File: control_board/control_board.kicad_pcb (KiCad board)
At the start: 2 copper layers, 50.8 x 76.2 mm, 38 parts, among them J1 Conn_01x08_Male, K1 G5Q-1A, Q1 Q_NPN_BEC, U1 MC78M05_TO252, U2 TSR_1-24120, U3 74LS02, U4 74LS02, U5 Conn_01x08_Male

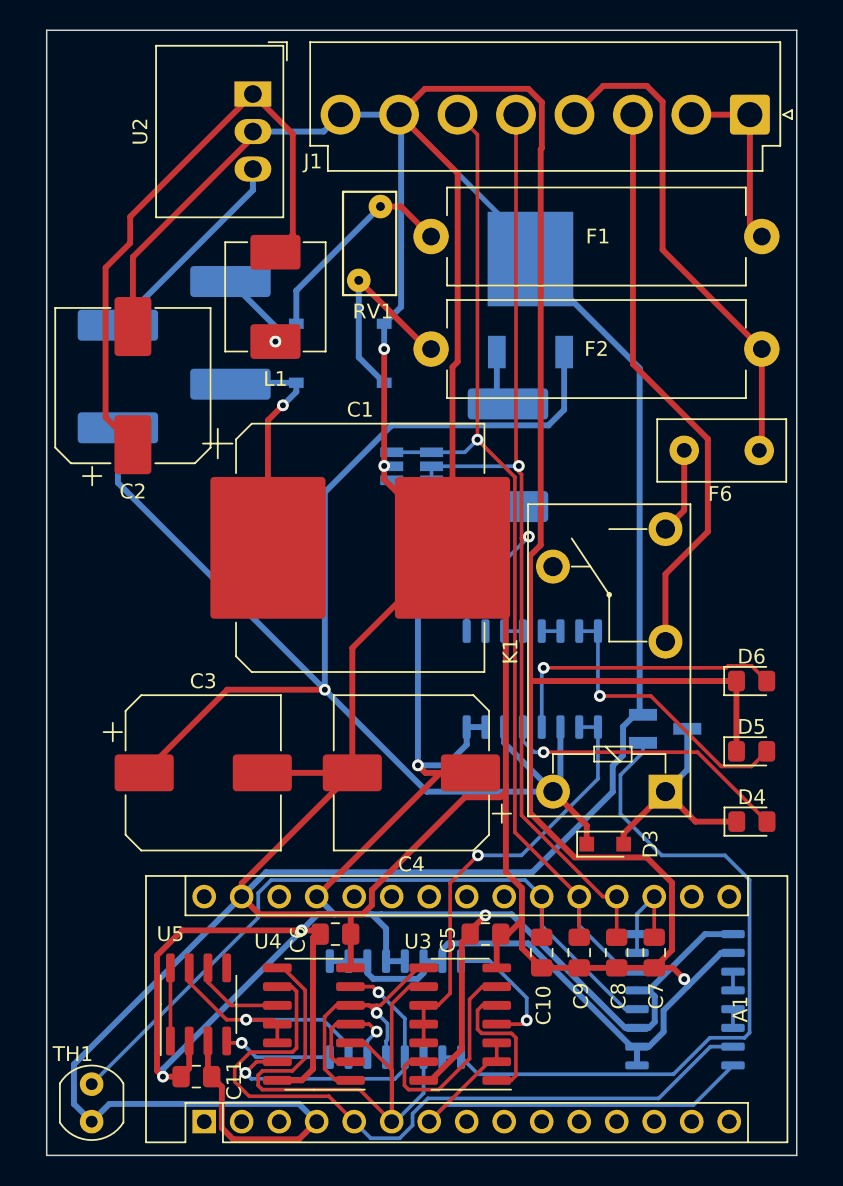
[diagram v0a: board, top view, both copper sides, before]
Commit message: Optimize some traces
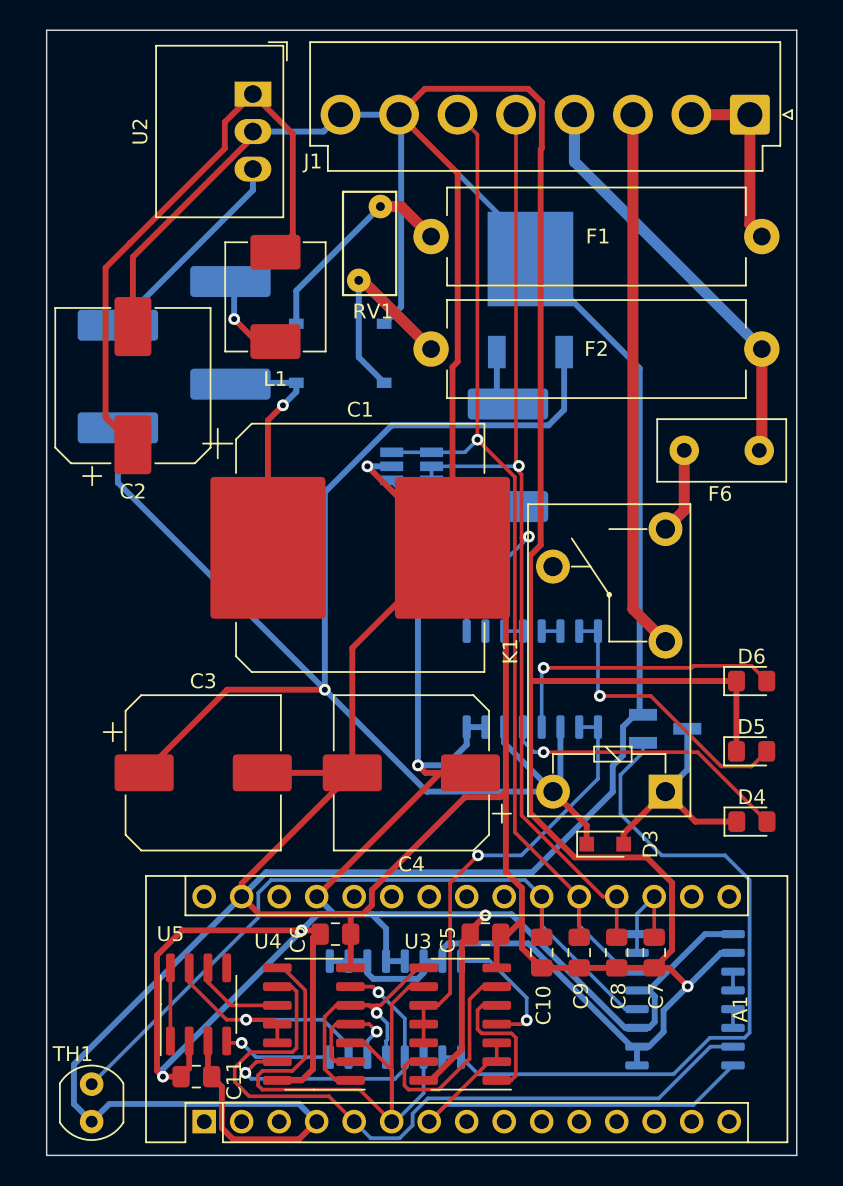
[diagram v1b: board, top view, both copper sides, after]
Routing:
- net GND: track 464.1 -> 456.0 mm, vias 3 -> 2
- net AC: track 33.7 -> 28.1 mm
- net /contactor_b: track 39.0 -> 36.6 mm
- net /hv_05: track 5.33 -> 6.07 mm

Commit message: Add actual mount holes
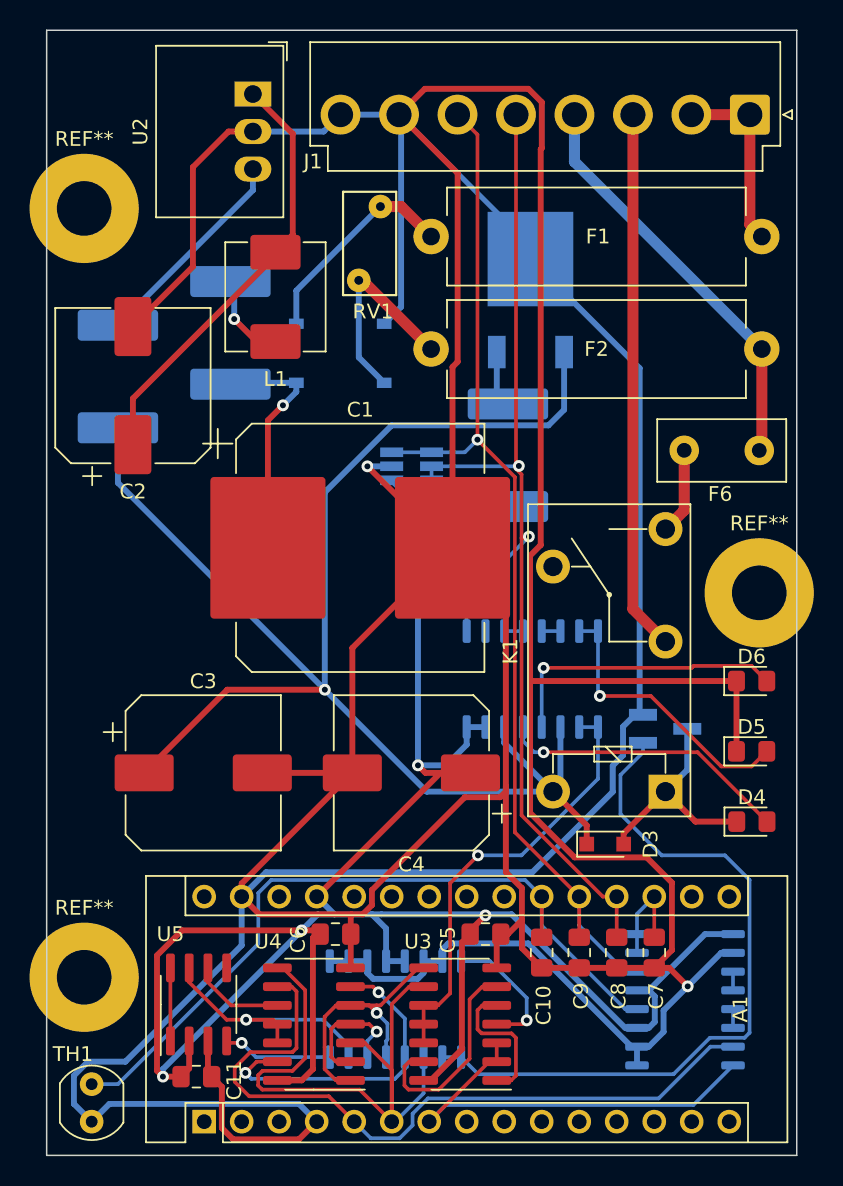
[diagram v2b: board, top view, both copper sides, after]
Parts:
- added REF**: MountingHole_3.7mm_Pad, MountingHole:MountingHole_3.7mm_Pad, F.Cu at (113.0, 36.2)
- added REF**: MountingHole_3.7mm_Pad, MountingHole:MountingHole_3.7mm_Pad, F.Cu at (113.0, 88.3)
- added REF**: MountingHole_3.7mm_Pad, MountingHole:MountingHole_3.7mm_Pad, F.Cu at (158.8, 62.2)
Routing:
- net /hv_06: track 41.0 -> 29.4 mm
- net GND: track 456.0 -> 458.4 mm
- net Net-(A1-Pad21): track 51.2 -> 52.2 mm
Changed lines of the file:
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@@
     (thickness 1.6)
     (drawings 11)
-    (tracks 460)
+    (tracks 461)
     (zones 0)
-    (modules 38)
+    (modules 41)
     (nets 64)
   )
@@
     (0 F.Cu signal)
     (31 B.Cu signal)
-    (32 B.Adhes user)
-    (33 F.Adhes user)
+    (32 B.Adhes user hide)
+    (33 F.Adhes user hide)
     (34 B.Paste user hide)
     (35 F.Paste user hide)
@@
     (40 Dwgs.User user)
     (41 Cmts.User user)
-    (42 Eco1.User user)
-    (43 Eco2.User user)
+    (42 Eco1.User user hide)
+    (43 Eco2.User user hide)
     (44 Edge.Cuts user)
     (45 Margin user)
@@
     (add_net GNDPWR)
   )
+  (module MountingHole:MountingHole_3.7mm_Pad (layer F.Cu)
+    (at 113.03 36.195)
+    (descr "Mounting Hole 3.7mm")
+    (tags "mounting hole 3.7mm")
+    (attr virtual)
+    (fp_text reference REF** (at 0 -4.7) (layer F.SilkS)
+      (effects (font (size 1 1) (thickness 0.15)))
+    )
+    (fp_text value MountingHole_3.7mm_Pad (at 0 4.7) (layer F.Fab)
+      (effects (font (size 1 1) (thickness 0.15)))
+    )
+    (fp_text user %R (at 0.3 0) (layer F.Fab)
+      (effects (font (size 1 1) (thickness 0.15)))
+    )
+    (fp_circle (center 0 0) (end 3.7 0) (layer Cmts.User) (width 0.15))
+    (fp_circle (center 0 0) (end 3.95 0) (layer F.CrtYd) (width 0.05))
+    (pad 1 thru_hole circle (at 0 0) (size 7.4 7.4) (drill 3.7) (layers *.Cu *.Mask))
+  )
+  (module MountingHole:MountingHole_3.7mm_Pad (layer F.Cu)
+    (at 113.03 88.265)
+    (descr "Mounting Hole 3.7mm")
+    (tags "mounting hole 3.7mm")
+    (attr virtual)
+    (fp_text reference REF** (at 0 -4.7) (layer F.SilkS)
+      (effects (font (size 1 1) (thickness 0.15)))
+    )
+    (fp_text value MountingHole_3.7mm_Pad (at 0 4.7) (layer F.Fab)
+      (effects (font (size 1 1) (thickness 0.15)))
+    )
+    (fp_circle (center 0 0) (end 3.95 0) (layer F.CrtYd) (width 0.05))
+    (fp_circle (center 0 0) (end 3.7 0) (layer Cmts.User) (width 0.15))
+    (fp_text user %R (at 0.3 0) (layer F.Fab)
+      (effects (font (size 1 1) (thickness 0.15)))
+    )
+    (pad 1 thru_hole circle (at 0 0) (size 7.4 7.4) (drill 3.7) (layers *.Cu *.Mask))
+  )
+  (module MountingHole:MountingHole_3.7mm_Pad (layer F.Cu)
+    (at 158.75 62.23)
+    (descr "Mounting Hole 3.7mm")
+    (tags "mounting hole 3.7mm")
+    (attr virtual)
+    (fp_text reference REF** (at 0 -4.7) (layer F.SilkS)
+      (effects (font (size 1 1) (thickness 0.15)))
+    )
+    (fp_text value MountingHole_3.7mm_Pad (at 0 4.7) (layer F.Fab)
+      (effects (font (size 1 1) (thickness 0.15)))
+    )
+    (fp_text user %R (at 0.3 0) (layer F.Fab)
+      (effects (font (size 1 1) (thickness 0.15)))
+    )
+    (fp_circle (center 0 0) (end 3.7 0) (layer Cmts.User) (width 0.15))
+    (fp_circle (center 0 0) (end 3.95 0) (layer F.CrtYd) (width 0.05))
+    (pad 1 thru_hole circle (at 0 0) (size 7.4 7.4) (drill 3.7) (layers *.Cu *.Mask))
+  )
   (module Resistor_THT:R_Axial_Power_L20.0mm_W6.4mm_P22.40mm (layer F.Cu)
     (at 136.525 38.1)
@@
   (segment (start 130.395 29.845) (end 129.252 30.988) (width 0.4) (layer B.Cu) (net 7) (status 10))
   (segment (start 130.395 29.845) (end 134.355 29.845) (width 0.4) (layer B.Cu) (net 7) (status 30))
-  (segment (start 124.46 31.360219) (end 124.46 30.988) (width 0.4) (layer F.Cu) (net 7) (status 30))
-  (segment (start 116.332 39.488219) (end 124.46 31.360219) (width 0.4) (layer F.Cu) (net 7) (status 20))
-  (segment (start 116.332 44.196) (end 116.332 39.488219) (width 0.4) (layer F.Cu) (net 7) (status 10))
   (segment (start 138.325001 33.815001) (end 134.355 29.845) (width 0.4) (layer F.Cu) (net 7) (status 20))
   (segment (start 138.325001 46.584001) (end 138.325001 33.815001) (width 0.4) (layer F.Cu) (net 7))
@@
   (segment (start 141.59201 75.29801) (end 141.59201 62.79801) (width 0.4) (layer F.Cu) (net 7))
   (segment (start 112.337999 96.843999) (end 113.538 98.044) (width 0.4) (layer B.Cu) (net 7))
-  (segment (start 112.337999 94.164001) (end 112.337999 96.843999) (width 0.4) (layer B.Cu) (net 7))
-  (segment (start 123.698 82.804) (end 112.337999 94.164001) (width 0.4) (layer B.Cu) (net 7))
   (segment (start 141.732 85.344) (end 142.678001 84.397999) (width 0.4) (layer F.Cu) (net 7))
   (segment (start 141.2455 85.344) (end 141.732 85.344) (width 0.4) (layer F.Cu) (net 7))
@@
   (segment (start 152.654 87.63) (end 153.905 88.881) (width 0.4) (layer F.Cu) (net 7))
   (segment (start 151.638 87.63) (end 152.654 87.63) (width 0.4) (layer F.Cu) (net 7))
+  (segment (start 116.332 44.196) (end 120.396 40.132) (width 0.4) (layer F.Cu) (net 7))
+  (segment (start 122.81 30.988) (end 124.46 30.988) (width 0.4) (layer F.Cu) (net 7))
+  (segment (start 120.396 33.402) (end 122.81 30.988) (width 0.4) (layer F.Cu) (net 7))
+  (segment (start 120.396 40.132) (end 120.396 33.402) (width 0.4) (layer F.Cu) (net 7))
+  (segment (start 112.337999 94.927999) (end 113.285998 93.98) (width 0.4) (layer B.Cu) (net 7))
+  (segment (start 112.337999 96.843999) (end 112.337999 94.927999) (width 0.4) (layer B.Cu) (net 7))
+  (segment (start 113.285998 93.98) (end 115.824 93.98) (width 0.4) (layer B.Cu) (net 7))
+  (segment (start 123.698 86.106) (end 123.698 82.804) (width 0.4) (layer B.Cu) (net 7))
+  (segment (start 115.824 93.98) (end 123.698 86.106) (width 0.4) (layer B.Cu) (net 7))
   (segment (start 139.664999 31.194999) (end 139.664999 51.857809) (width 0.25) (layer F.Cu) (net 8))
   (segment (start 138.315 29.845) (end 139.664999 31.194999) (width 0.25) (layer F.Cu) (net 8) (status 10))
@@
   (segment (start 144.018 84.77) (end 144.018 82.804) (width 0.25) (layer B.Cu) (net 10))
   (segment (start 150.472 90.424) (end 149.672 90.424) (width 0.25) (layer B.Cu) (net 10))
-  (segment (start 124.823001 82.553997) (end 124.823001 84.218999) (width 0.25) (layer B.Cu) (net 10))
-  (segment (start 125.697999 81.678999) (end 124.823001 82.553997) (width 0.25) (layer B.Cu) (net 10))
-  (segment (start 124.823001 84.218999) (end 113.538 95.504) (width 0.25) (layer B.Cu) (net 10))
-  (segment (start 142.892999 81.678999) (end 125.697999 81.678999) (width 0.25) (layer B.Cu) (net 10))
-  (segment (start 144.018 82.804) (end 142.892999 81.678999) (width 0.25) (layer B.Cu) (net 10))
+  (segment (start 125.697999 81.678999) (end 142.892999 81.678999) (width 0.25) (layer B.Cu) (net 10))
+  (segment (start 124.823001 82.553997) (end 125.697999 81.678999) (width 0.25) (layer B.Cu) (net 10))
+  (segment (start 124.823001 85.996999) (end 124.823001 82.553997) (width 0.25) (layer B.Cu) (net 10))
+  (segment (start 142.892999 81.678999) (end 144.018 82.804) (width 0.25) (layer B.Cu) (net 10))
+  (segment (start 115.316 95.504) (end 124.823001 85.996999) (width 0.25) (layer B.Cu) (net 10))
+  (segment (start 113.538 95.504) (end 115.316 95.504) (width 0.25) (layer B.Cu) (net 10))
   (segment (start 133.858 90.087) (end 133.858 98.044) (width 0.25) (layer F.Cu) (net 11))
   (segment (start 135.045 88.9) (end 133.858 90.087) (width 0.25) (layer F.Cu) (net 11))
@@
   (segment (start 127.4 48.622) (end 126.492 49.53) (width 0.4) (layer B.Cu) (net 46))
   (segment (start 127.4 48.006) (end 127.4 48.622) (width 0.4) (layer B.Cu) (net 46) (status 10))
-  (segment (start 114.48199 50.34599) (end 116.332 52.196) (width 0.4) (layer F.Cu) (net 47) (status 20))
-  (segment (start 114.48199 40.206845) (end 114.48199 50.34599) (width 0.4) (layer F.Cu) (net 47))
-  (segment (start 116.145711 38.543124) (end 114.48199 40.206845) (width 0.4) (layer F.Cu) (net 47))
   (segment (start 127.159 37.987) (end 125.984 39.162) (width 0.4) (layer F.Cu) (net 47) (status 30))
   (segment (start 127.159 31.147) (end 127.159 37.987) (width 0.4) (layer F.Cu) (net 47) (status 20))
   (segment (start 124.46 28.448) (end 127.159 31.147) (width 0.4) (layer F.Cu) (net 47) (status 10))
-  (segment (start 116.145711 38.543124) (end 116.145711 38.540289) (width 0.4) (layer F.Cu) (net 47))
-  (segment (start 122.555 32.131) (end 122.555 30.353) (width 0.4) (layer F.Cu) (net 47))
-  (segment (start 116.145711 38.540289) (end 122.555 32.131) (width 0.4) (layer F.Cu) (net 47))
-  (segment (start 124.46 28.448) (end 122.555 30.353) (width 0.4) (layer F.Cu) (net 47))
+  (segment (start 125.984 39.413998) (end 125.984 39.162) (width 0.4) (layer F.Cu) (net 47))
+  (segment (start 116.332 49.065998) (end 125.984 39.413998) (width 0.4) (layer F.Cu) (net 47))
+  (segment (start 116.332 52.196) (end 116.332 49.065998) (width 0.4) (layer F.Cu) (net 47))
   (segment (start 133.096 36.068) (end 127.4 41.764) (width 0.4) (layer B.Cu) (net 48) (status 10))
   (segment (start 127.4 41.764) (end 127.4 44.006) (width 0.4) (layer B.Cu) (net 48) (status 20))

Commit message: Ground plane via stitching
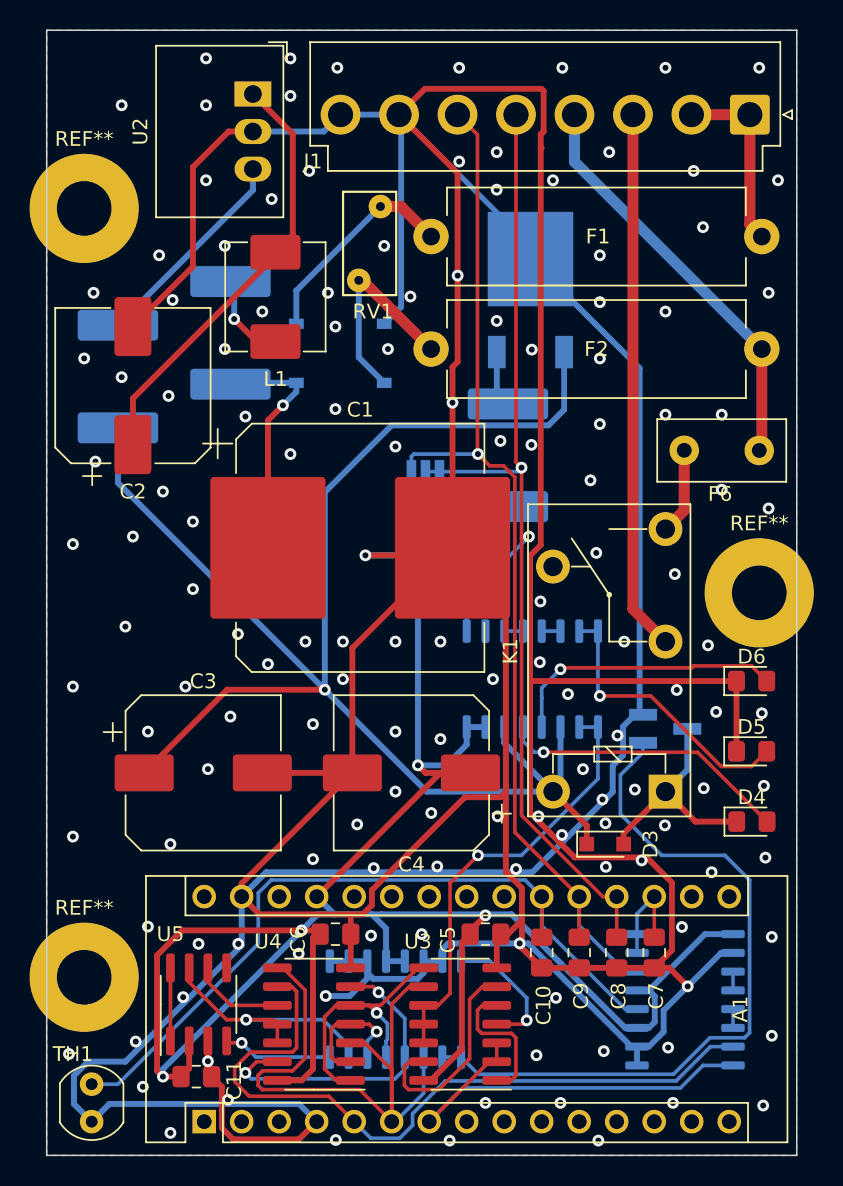
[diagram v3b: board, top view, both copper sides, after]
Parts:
- moved D2 1.95 mm to (136.1, 55.4), turned to 90 degrees
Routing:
- net GND: track 458.4 -> 467.1 mm, vias 2 -> 144
- net +5V: track 160.7 -> 156.9 mm
- net /sensor_a: track 72.5 -> 75.1 mm
- net Net-(D6-Pad2): track 19.7 -> 18.9 mm
- added copper zone on B.Cu, net GND
- added copper zone on F.Cu, net GND
